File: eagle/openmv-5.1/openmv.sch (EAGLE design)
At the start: 52 parts, among them U1 OV9650, U11 ADP222, U2 USD-47571, U4 STM32F407LQFP100, U5 BEAD, U6 BEAD, U7 24FC128, X1 USB-MICROB

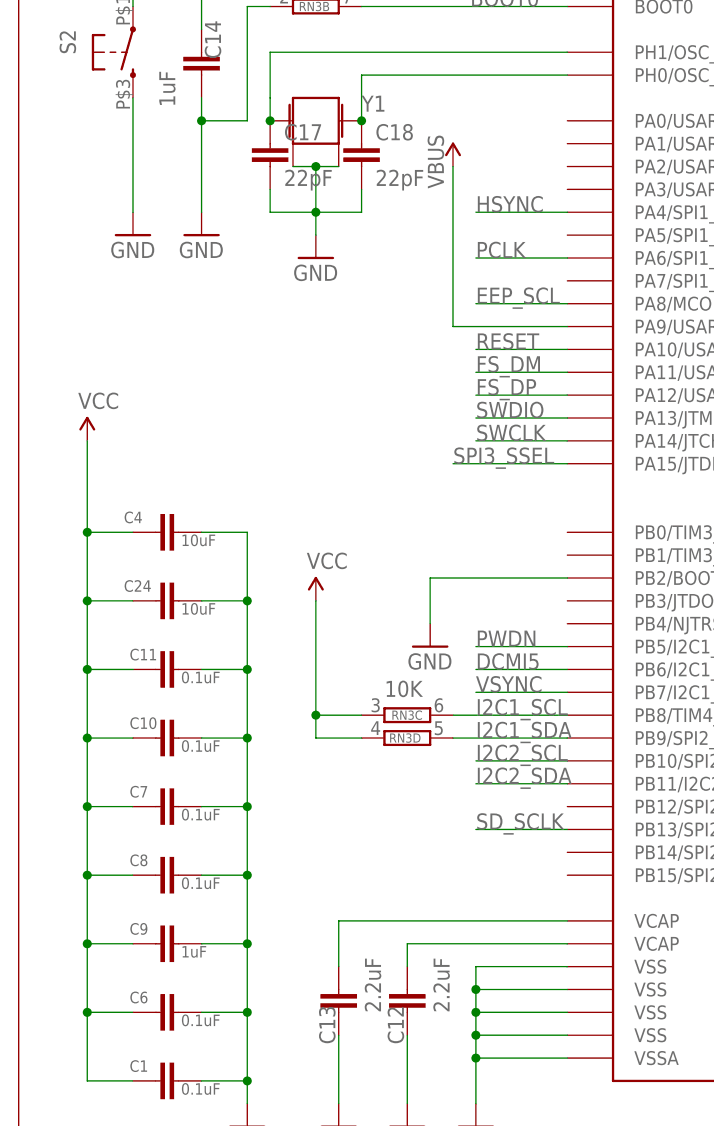
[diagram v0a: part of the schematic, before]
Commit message: Fix components values
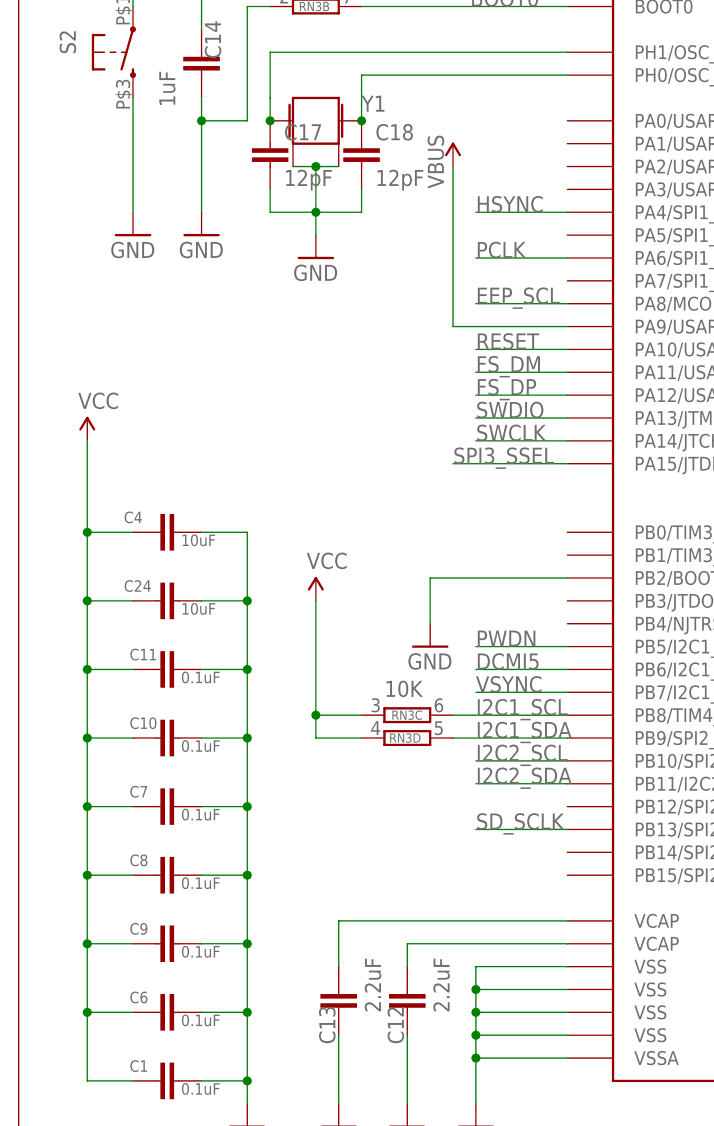
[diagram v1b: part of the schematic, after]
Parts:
- C17, C18: value 22pF -> 12pF
- C9: value 1uF -> 0.1uF
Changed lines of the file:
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@@
 <part name="P+13" library="SparkFun" deviceset="VCC" device=""/>
 <part name="Y1" library="mux" deviceset="CRYSTAL" device="2.5X2.0"/>
-<part name="C17" library="sfe" deviceset="CAP" device="0402-CAP" value="22pF"/>
-<part name="C18" library="sfe" deviceset="CAP" device="0402-CAP" value="22pF"/>
-<part name="C9" library="sfe" deviceset="CAP" device="0402-CAP" value="1uF"/>
+<part name="C17" library="sfe" deviceset="CAP" device="0402-CAP" value="12pF"/>
+<part name="C18" library="sfe" deviceset="CAP" device="0402-CAP" value="12pF"/>
+<part name="C9" library="sfe" deviceset="CAP" device="0402-CAP" value="0.1uF"/>
 <part name="SJ1" library="sfe" deviceset="SOLDERJUMPER" device="TRACE"/>
 <part name="JP3" library="mux" deviceset="PINHD-1X2" device=""/>
